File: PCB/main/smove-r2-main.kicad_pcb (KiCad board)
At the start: 4 copper layers, 25 x 30 mm, 47 parts, among them J1 TYPE-C-31-M-12, J2 Battery wire pads 2.54mm, SW2 RESET, SW3 BOOT / USER, U1 ESP32-C3-MINI-1-N4, U2 ICM-20948, U3 PCA9306DCUR, U4 AP2112K-3.3TRG1, U5 AP2112K-1.8TRG1, U6 BQ24074RGTR, U8 USBLC6-2SC6, U9 PESD5V0S2BT,215

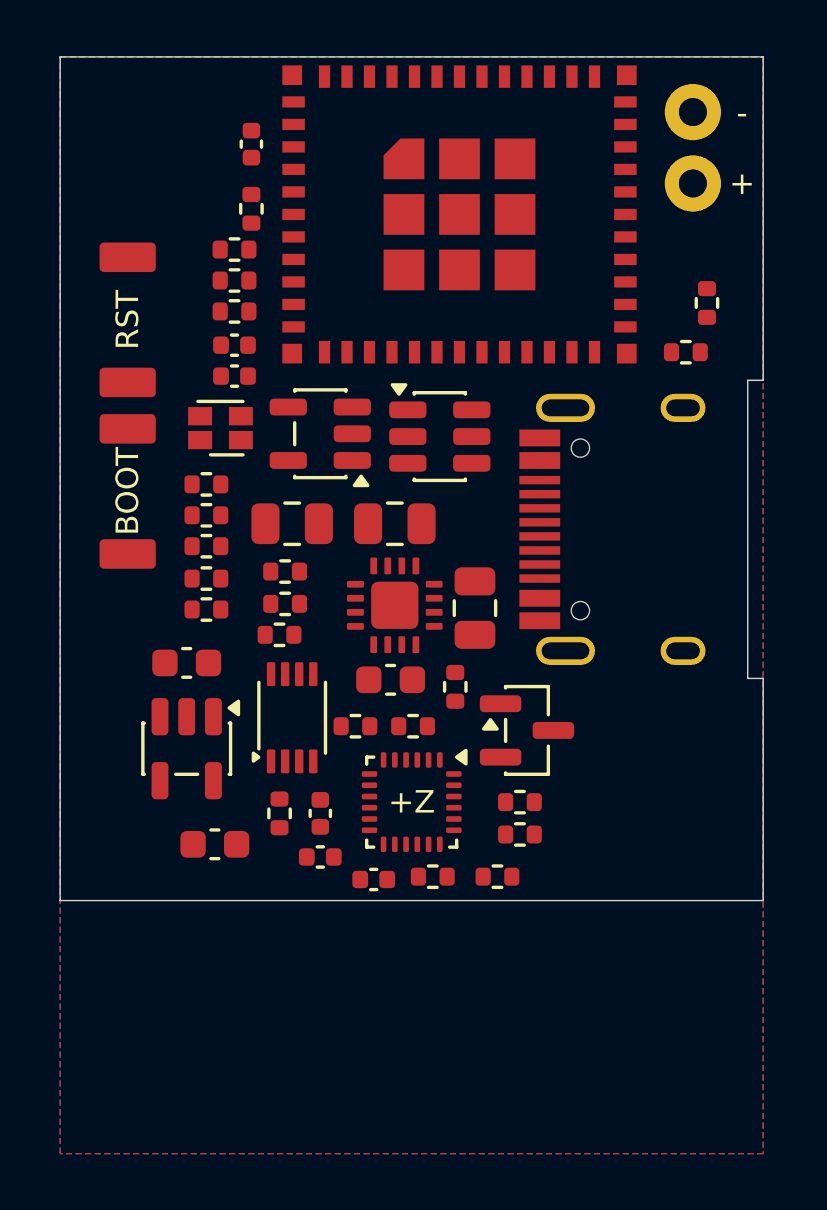
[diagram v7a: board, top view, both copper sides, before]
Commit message: Add some decent routing.
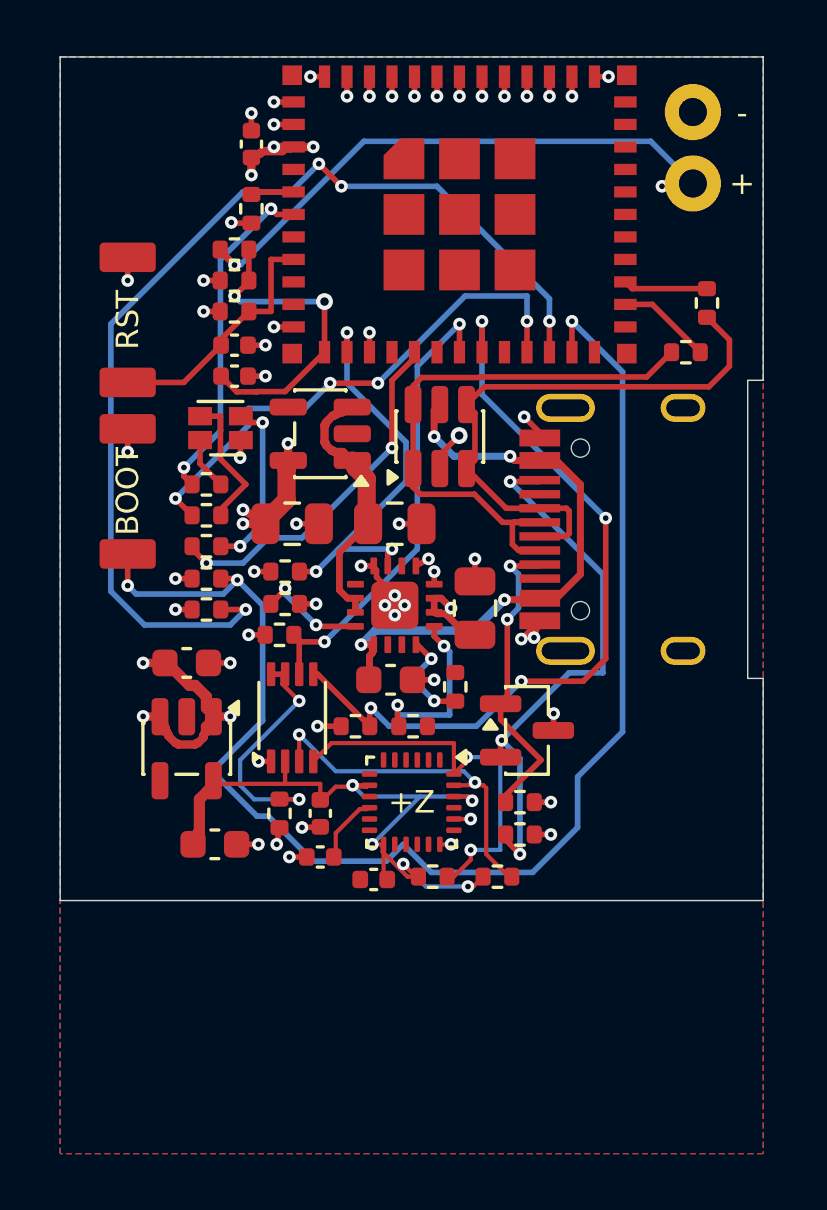
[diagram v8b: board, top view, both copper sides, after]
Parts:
- turned C7 to 180 degrees
- turned U8 to 90 degrees
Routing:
- net Net-(U1-GPIO9_/_BOOT): track 0.00 -> 50.0 mm, vias 0 -> 3
- net /Compute/STRAP8: track 0.00 -> 37.8 mm, vias 0 -> 4
- net GND: track 0.00 -> 32.5 mm, vias 0 -> 49
- net /SDA_HOST: track 0.00 -> 28.0 mm, vias 0 -> 4
- net /IMU/1V8_IMU: track 0.00 -> 25.4 mm, vias 0 -> 5
- net /Power/PACK_P: track 0.00 -> 23.7 mm, vias 0 -> 3
- net /3V3_MAIN: track 0.00 -> 22.2 mm, vias 0 -> 18
- net /USB_DM: track 0.00 -> 21.1 mm
- net /VBUS: track 0.00 -> 20.9 mm, vias 0 -> 4
- net /USB_DP: track 0.00 -> 20.7 mm
- net /USB/CC2: track 0.00 -> 19.7 mm, vias 0 -> 3
- net /Compute/LED_G: track 0.00 -> 18.7 mm, vias 0 -> 4
- net /SCL_HOST: track 0.00 -> 17.0 mm, vias 0 -> 2
- net /USB_POWER_N: track 0.00 -> 14.5 mm, vias 0 -> 3
- net /IMU/SDA_1V8: track 0.00 -> 14.1 mm, vias 0 -> 2
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- added copper zone on In2.Cu, net /3V3_MAIN
- added copper zone on In2.Cu, net /Power/PACK_P
